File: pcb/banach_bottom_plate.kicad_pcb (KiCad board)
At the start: 2 copper layers, 132.3 x 90.7 mm, 6 parts

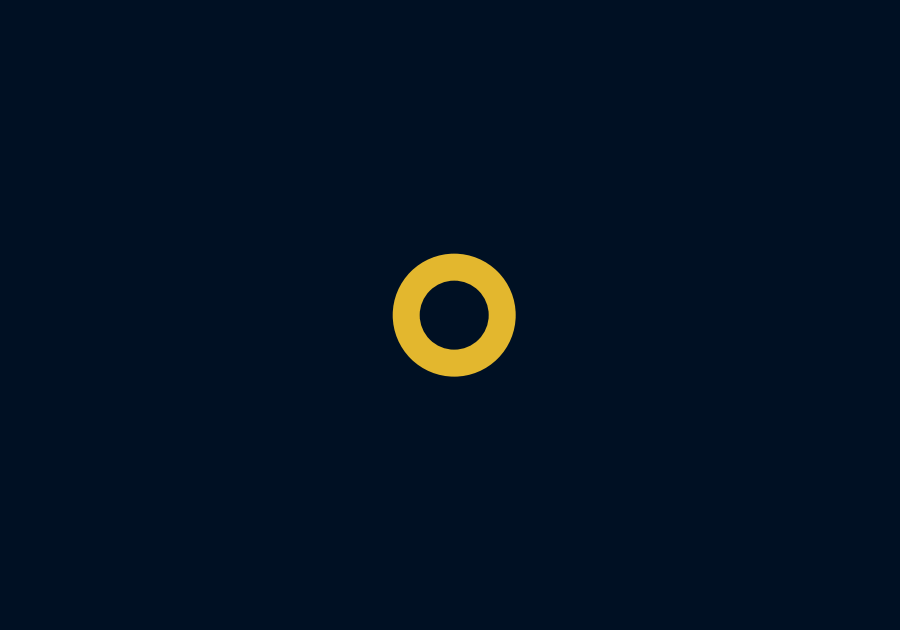
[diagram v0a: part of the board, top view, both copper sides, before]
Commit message: aligned column 0 to true choc spacing
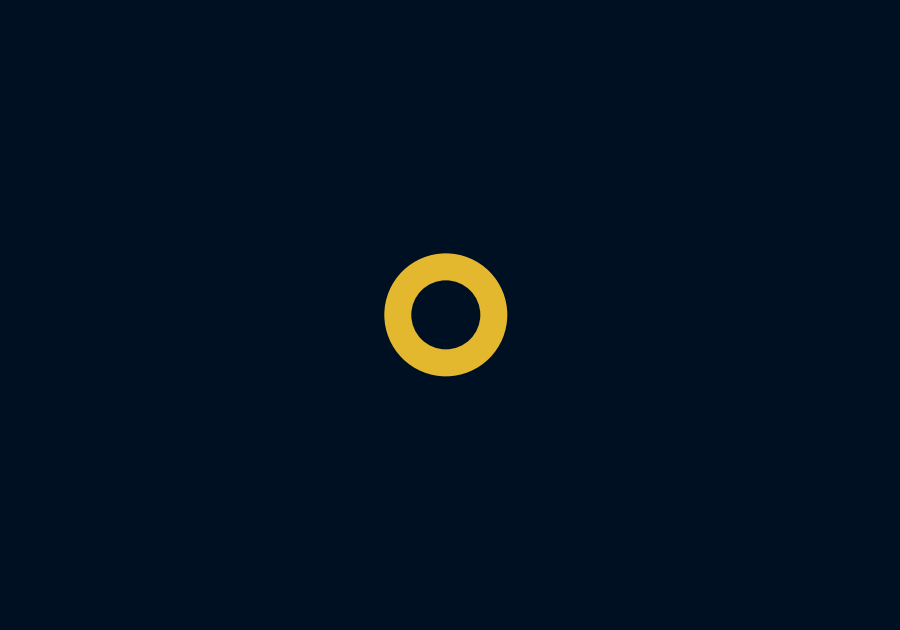
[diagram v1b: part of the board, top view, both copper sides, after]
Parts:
- moved h6 0.28 mm to (112.6, 66.9)
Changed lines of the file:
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@@
       (drillshape 0)
       (scaleselection 1)
-      (outputdirectory "gerber-plate/")
+      (outputdirectory "../gerber/")
     )
   )
@@
   )
   (footprint "kbd:M2_Threads_v2" (layer "F.Cu")
-    (at 112.91 66.9)
+    (at 112.63 66.89)
     (descr "Mounting Hole 2.2mm, no annular, M2")
     (tags "mounting hole 2.2mm no annular m2")
